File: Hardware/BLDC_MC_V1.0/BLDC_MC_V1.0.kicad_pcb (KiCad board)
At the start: 2 copper layers, 245 parts, among them J1 Conn_01x03_Pin, J2 Conn_01x03_Pin, J3 USB_C_Receptacle_USB2.0_16P, J4 Conn_02x03_Counter_Clockwise, J5 Conn_02x03_Counter_Clockwise, J6 1714971, J7 1714984, J8 430451012, Q1 BSC027N10NS5ATMA1, Q2 BSC027N10NS5ATMA1, Q3 BSC027N10NS5ATMA1, Q4 BSC027N10NS5ATMA1, Q5 BSC027N10NS5ATMA1, Q6 BSC027N10NS5ATMA1, Q7 BSC027N10NS5ATMA1, SW1 SW_Push, U1 LM76005RNPR, U10 TLV9061IDBVR, U11 TLV9061IDBVR, U12 TLV9061IDBVR, U13 TLV9061IDBVR, U14 TLV9061IDBVR, U15 TLV9061IDBVR, U16 LM74700QDRQ1, U2 TCAN334DR, U3 TLV9061IDBVR, U4 STM32G431RBT6, U5 LDL1117S33R, U6 DRV8353HRTAR, U7 NCV4274ADT50RKG, U8 25LC256-E_SN, U9 USBLC6-2SC6, Y1 7M-24.000MAAJ-T, Y2 ABS07-32.768KHZ-T

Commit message: Run DRC and solve all errors and warnings (project updated to Kicad 10)
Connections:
- J3 pad S1: GND -> (no net)

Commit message: Update recovery files of the project
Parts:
- removed TP11, TP12, TP13, TP14, TP15, TP16: TestPoint, Connector_Pin:Pin_D0.9mm_L10.0mm_W2.4mm_FlatFork
- moved Q6 154.0 mm to (129.2, 27.2), turned to 180 degrees
- moved R7 144.6 mm to (137.4, 33.5), turned to -90 degrees
- moved Q5 136.6 mm to (128.9, 41.3), turned to 180 degrees
- moved C65 132.3 mm to (228.6, 103.4)
- moved C66 132.3 mm to (235.7, 129.8)
- moved C84 132.3 mm to (244.6, 129.8)
- moved R26 132.3 mm to (214.1, 119.5)
- moved R29 132.3 mm to (214.1, 127.0)
- moved R32 132.3 mm to (218.1, 119.5)
- moved R56 132.3 mm to (235.5, 119.5)
- moved R60 132.3 mm to (235.5, 127.0)
- moved TP6 132.3 mm to (205.9, 119.0)
- moved TP7 132.3 mm to (205.9, 122.9)
- moved C10 132.3 mm to (161.9, 50.4)
- moved C12 132.3 mm to (253.4, 103.9)
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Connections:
- net Net-(C16-Pad1) renamed /BLDC_MC_V1.0_CAN_Transceiver/Split_CAP
- net Net-(U2-CANH) renamed /BLDC_MC_V1.0_CAN_Transceiver/CANH
- net Net-(U2-CANL) renamed /BLDC_MC_V1.0_CAN_Transceiver/CANL
- net Net-(U2-RXD) renamed /BLDC_MC_V1.0_CAN_Transceiver/IC_RXD
- net Net-(U2-SHDN) renamed /BLDC_MC_V1.0_CAN_Transceiver/SHDN
- net Net-(U2-STB) renamed /BLDC_MC_V1.0_CAN_Transceiver/STB
- net Net-(U2-TXD) renamed /BLDC_MC_V1.0_CAN_Transceiver/IC_TXD
- net Net-(U8-SI) renamed /BLDC_MC_V1.0_Memory/SI
- net Net-(U8-SO) renamed /BLDC_MC_V1.0_Memory/SO
- net Net-(U8-~CS) renamed /BLDC_MC_V1.0_Memory/CS
- net Net-(U8-~HOLD) renamed /BLDC_MC_V1.0_Memory/NHOLD
- net Net-(U8-~WP) renamed /BLDC_MC_V1.0_Memory/NWP
- R44 pad 1: /BLDC_MC_V1.0_MCU/SCK -> /BLDC_MC_V1.0_Memory/SCK
- R44 pad 2: Net-(U8-SCK) -> /BLDC_MC_V1.0_Memory/SCK
- U4 pad 19: /BLDC_MC_V1.0_MCU/SCK -> /BLDC_MC_V1.0_Memory/SCK
- U8 pad 6: Net-(U8-SCK) -> /BLDC_MC_V1.0_Memory/SCK
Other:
- board outline added: 131.4 x 64.3 mm
- copper layers 2 -> 8

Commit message: Update the plaacement of PCB
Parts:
- moved C11 220.5 mm to (38.4, 28.1)
- moved C12 220.5 mm to (47.0, 26.1)
- moved C13 220.5 mm to (38.1, 15.3)
- moved C14 220.5 mm to (38.1, 17.8)
- moved C15 220.5 mm to (38.1, 20.3)
- moved C16 220.5 mm to (38.1, 22.8)
- moved R9 220.5 mm to (38.1, 25.3)
- moved CR1 220.5 mm to (42.3, 28.1)
- moved R10 220.5 mm to (42.2, 15.3)
- moved R11 220.5 mm to (42.2, 17.8)
- moved R12 220.5 mm to (42.2, 20.3)
- moved R13 220.5 mm to (42.2, 22.8)
- moved R14 220.5 mm to (42.2, 25.3)
- moved FL1 216.4 mm to (52.7, 20.8), turned to 180 degrees
- moved U2 209.0 mm to (59.8, 20.8), turned to 180 degrees
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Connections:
- R44 pad 1: /BLDC_MC_V1.0_Memory/SCK -> /BLDC_MC_V1.0_MCU/SCK
- R44 pad 2: /BLDC_MC_V1.0_Memory/SCK -> /BLDC_MC_V1.0_Memory/SCK_M
- U4 pad 19: /BLDC_MC_V1.0_Memory/SCK -> /BLDC_MC_V1.0_MCU/SCK
- U8 pad 6: /BLDC_MC_V1.0_Memory/SCK -> /BLDC_MC_V1.0_Memory/SCK_M
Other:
- board size 131.4 x 64.3 mm -> 131.4 x 99.9 mm

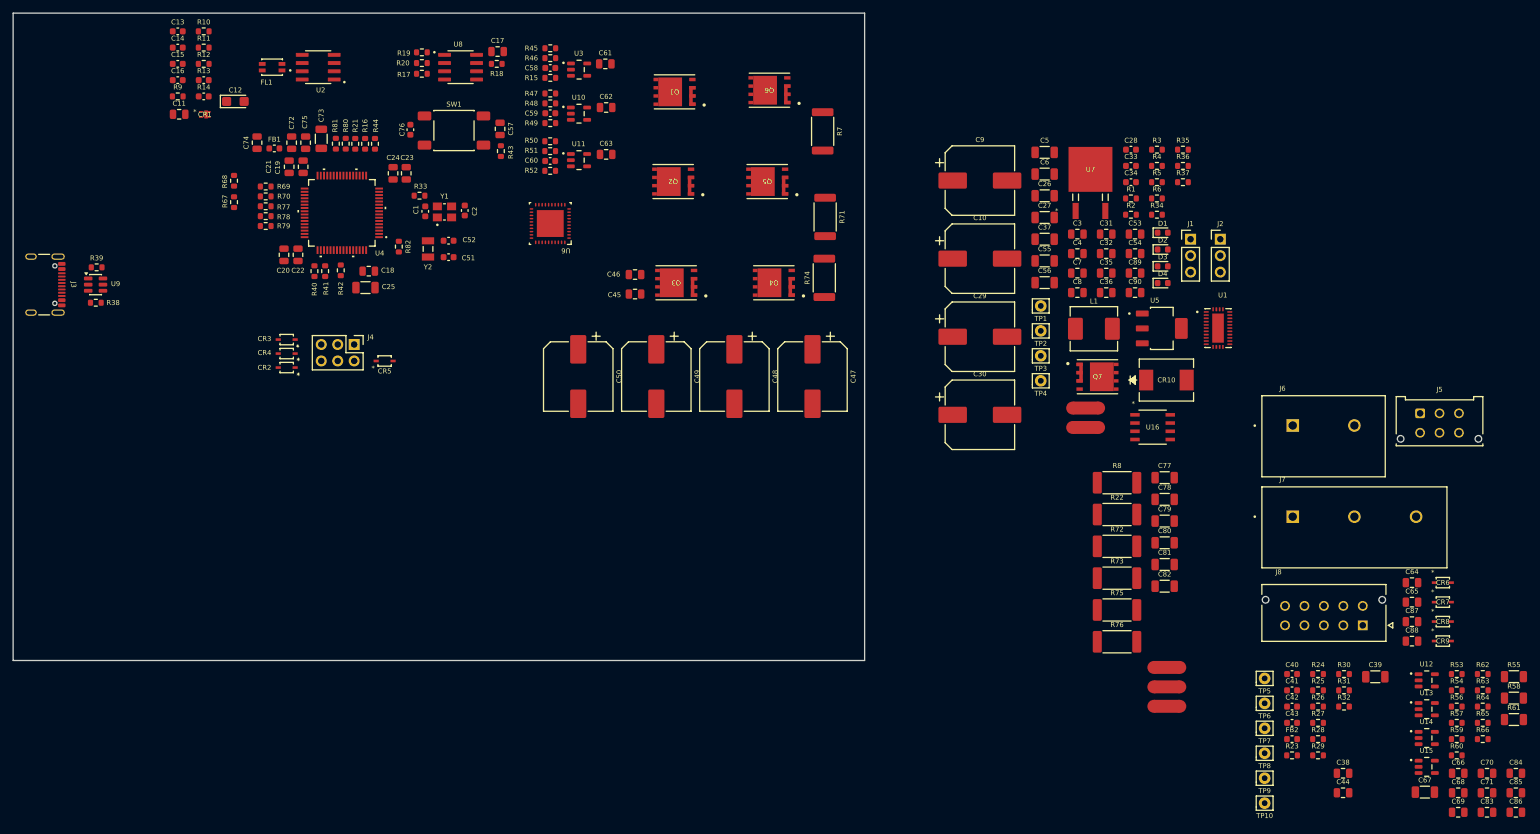
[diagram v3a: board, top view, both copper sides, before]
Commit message: Update the placement of the PCB
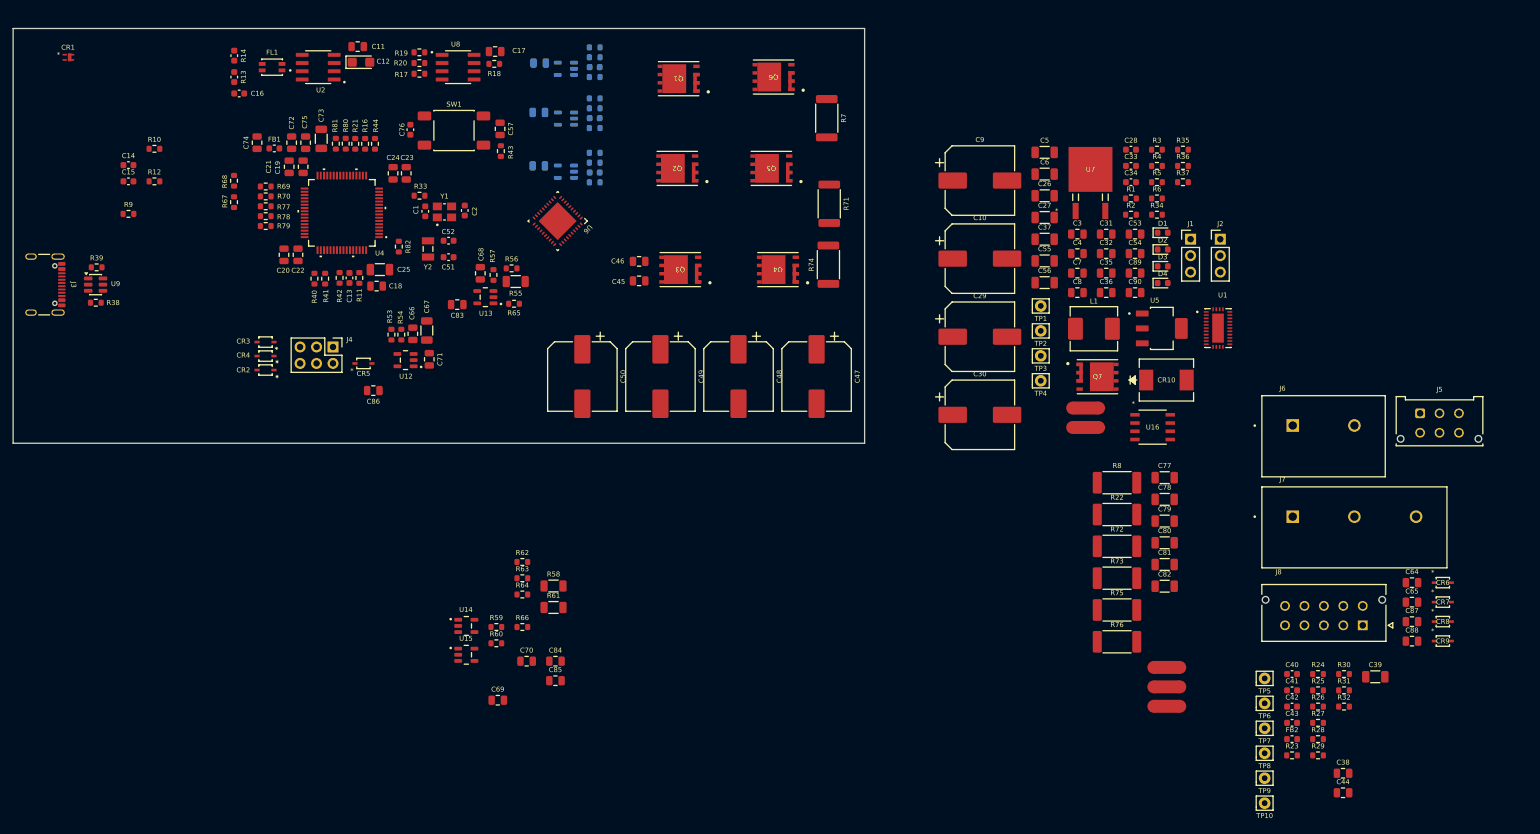
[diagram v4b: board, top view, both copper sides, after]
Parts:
- C58, C59, C60, C61, C62, C63, R15, R45, R46, R47, R48, R49, R50, R51, R52, U10, U11, U3: moved to B.Cu
- moved C86 187.9 mm to (68.3, 70.7), turned to 180 degrees
- moved C83 177.2 mm to (81.3, 57.5), turned to 180 degrees
- moved C71 176.4 mm to (77.0, 65.9), turned to 90 degrees
- moved C66 175.0 mm to (74.4, 62.0), turned to 90 degrees
- moved R53 172.6 mm to (71.1, 62.1), turned to 90 degrees
- moved R54 171.9 mm to (72.6, 62.1), turned to -90 degrees
- moved C68 170.9 mm to (84.8, 52.6), turned to 90 degrees
- moved C67 169.7 mm to (76.6, 61.5), turned to 90 degrees
- moved R55 165.7 mm to (90.3, 53.9), turned to 180 degrees
- moved U12 165.2 mm to (73.3, 66.0), turned to 180 degrees
- moved R57 163.9 mm to (86.9, 52.9), turned to 90 degrees
- moved R65 162.9 mm to (90.0, 57.3), turned to 180 degrees
- moved R56 160.8 mm to (89.7, 51.9)
- moved U13 158.6 mm to (85.6, 56.3), turned to 180 degrees
- moved C69 149.2 mm to (87.5, 118.5)
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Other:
- board size 131.4 x 99.9 mm -> 131.4 x 64 mm

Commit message: Update the placement of the board
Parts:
- removed TP10, TP5, TP6, TP7, TP8, TP9: TestPoint, Connector_Pin:Pin_D0.9mm_L10.0mm_W2.4mm_FlatFork
- C47, C48, C49, C50, C66, C67, C71, C86, R53, R54, U12: moved to B.Cu
- moved C44 158.0 mm to (96.5, 31.8), turned to 135 degrees
- moved R29 152.5 mm to (89.7, 38.9), turned to -45 degrees
- moved R28 151.0 mm to (87.7, 42.0)
- moved R32 150.1 mm to (95.4, 33.1), turned to -45 degrees
- moved R27 149.3 mm to (90.9, 37.7), turned to -45 degrees
- moved R31 149.2 mm to (93.2, 35.4), turned to -45 degrees
- moved R26 149.1 mm to (87.7, 40.5)
- moved R30 148.2 mm to (92.0, 36.6), turned to -45 degrees
- moved R25 145.6 mm to (94.3, 34.3), turned to -45 degrees
- moved R23 144.3 mm to (92.5, 43.6), turned to 45 degrees
- moved R24 142.4 mm to (91.3, 42.4), turned to 45 degrees
- moved C38 140.7 mm to (102.4, 49.4), turned to -45 degrees
- moved FB2 140.1 mm to (92.6, 48.3), turned to -45 degrees
- moved C39 135.9 mm to (104.5, 48.3), turned to 135 degrees
- moved C43 135.9 mm to (96.5, 47.5), turned to 45 degrees
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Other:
- board size 131.4 x 64 mm -> 137 x 50 mm

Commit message: Update the component placement of the board
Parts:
- removed C14, C15: 10pF, Capacitor_SMD:C_0603_1608Metric
- removed R10, R9: 33R, Resistor_SMD:R_0603_1608Metric
- added H1: MountingHole_Pad, MountingHole:MountingHole_2.2mm_M2_Pad_Via, F.Cu at (40.5, 65.4)
- added H2: MountingHole_Pad, MountingHole:MountingHole_2.2mm_M2_Pad_Via, F.Cu at (40.4, 16.8)
- added H3: MountingHole_Pad, MountingHole:MountingHole_2.2mm_M2_Pad_Via, F.Cu at (154.8, 65.5)
- added H4: MountingHole_Pad, MountingHole:MountingHole_2.2mm_M2_Pad_Via, F.Cu at (154.8, 16.8)
- C10, C17, C29, C30, C68, C69, C70, C83, C84, C85, C88, C9, CR7, CR8, CR9, R17, R18, R19, R20, R55, R56, R57, R58, R59, R60, R61, R62, R63, R64, R65, R66, U13, U14, U15, U8: moved to B.Cu
- J5: value Conn_02x03_Counter_Clockwise -> S6B-PH-K-S_LF__SN_; footprint Connector_Molex:Molex_Micro-Fit_3.0_43045-0612_2x03_P3.00mm_Vertical -> BLDC_Motor_Driver_Components_Footprint:JST_S6B-PH-K-S_LF__SN_
- J6: value 1714971 -> XT60-M; footprint BLDC_Motor_Driver_Components_Footprint:PHOENIX_1714971 -> BLDC_Motor_Driver_Components_Footprint:AMASS_XT60-M
- J8: value 430451012 -> S10B-PHDSS LFSN; footprint BLDC_Motor_Driver_Components_Footprint:MOLEX_430451012 -> BLDC_Motor_Driver_Components_Footprint:CONN_S10B-PHDSS_JST
- moved CR9 244.6 mm to (40.3, 46.4), turned to 180 degrees
- moved CR8 244.3 mm to (40.3, 44.3), turned to 180 degrees
- moved CR7 244.0 mm to (40.3, 42.2), turned to 180 degrees
- moved C88 242.7 mm to (40.1, 40.0), turned to 180 degrees
- moved C87 235.0 mm to (48.0, 38.2), turned to 90 degrees
- moved CR6 232.7 mm to (49.7, 46.4)
- moved J8 229.6 mm to (45.7, 40.2), turned to -90 degrees
- moved J6 219.8 mm to (42.4, 28.2), turned to -90 degrees
- moved C64 173.6 mm to (91.1, 109.3)
- moved C65 173.6 mm to (91.1, 112.4)
- moved C26 166.8 mm to (51.0, 87.5)
- moved C27 166.8 mm to (51.0, 90.9)
- moved C28 166.8 mm to (64.3, 80.4)
- moved C3 166.8 mm to (56.0, 93.4)
- moved C31 166.8 mm to (60.5, 93.4)
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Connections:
- C90 pad 2: /BLDC_MC_V1.0_Connectors/GND_In -> GND
- CR10 pad 2: /BLDC_MC_V1.0_Connectors/GND_In -> GND
- J5 pad 3: GND -> /BLDC_MC_V1.0_Connectors/Hall_B
- J5 pad 5: /BLDC_MC_V1.0_Connectors/Hall_B -> +3.3V
- J5 pad 6: +3.3V -> GND
- U16 pad 1: /BLDC_MC_V1.0_Connectors/GND_In -> GND
- U4 pad 58: /BLDC_MC_V1.0_CAN_Transceiver/CAN_STB -> /BLDC_MC_V1.0_CAN_Transceiver/STB
- U4 pad 59: /BLDC_MC_V1.0_CAN_Transceiver/CAN_SHDN -> /BLDC_MC_V1.0_CAN_Transceiver/SHDN
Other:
- board size 137 x 50 mm -> 120 x 55 mm

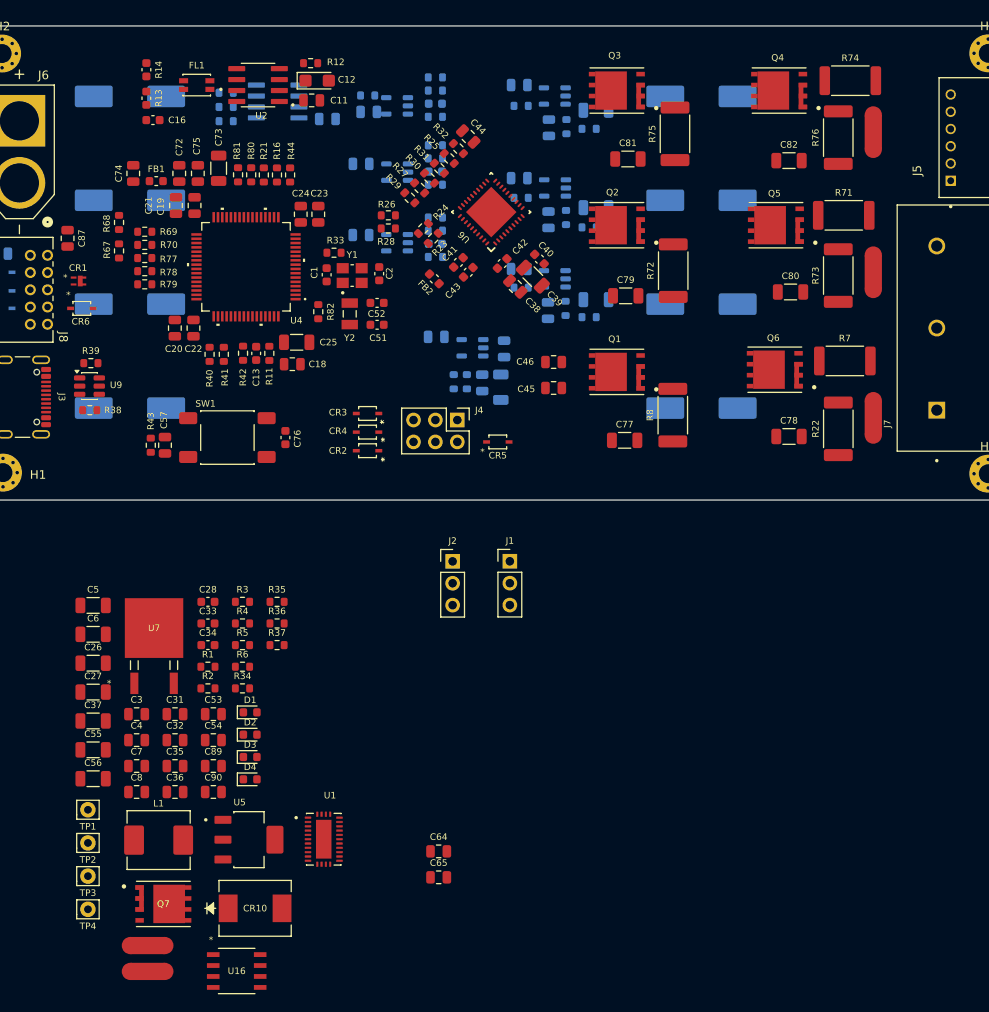
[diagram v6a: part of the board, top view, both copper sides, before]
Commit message: Update the components' placement of the board
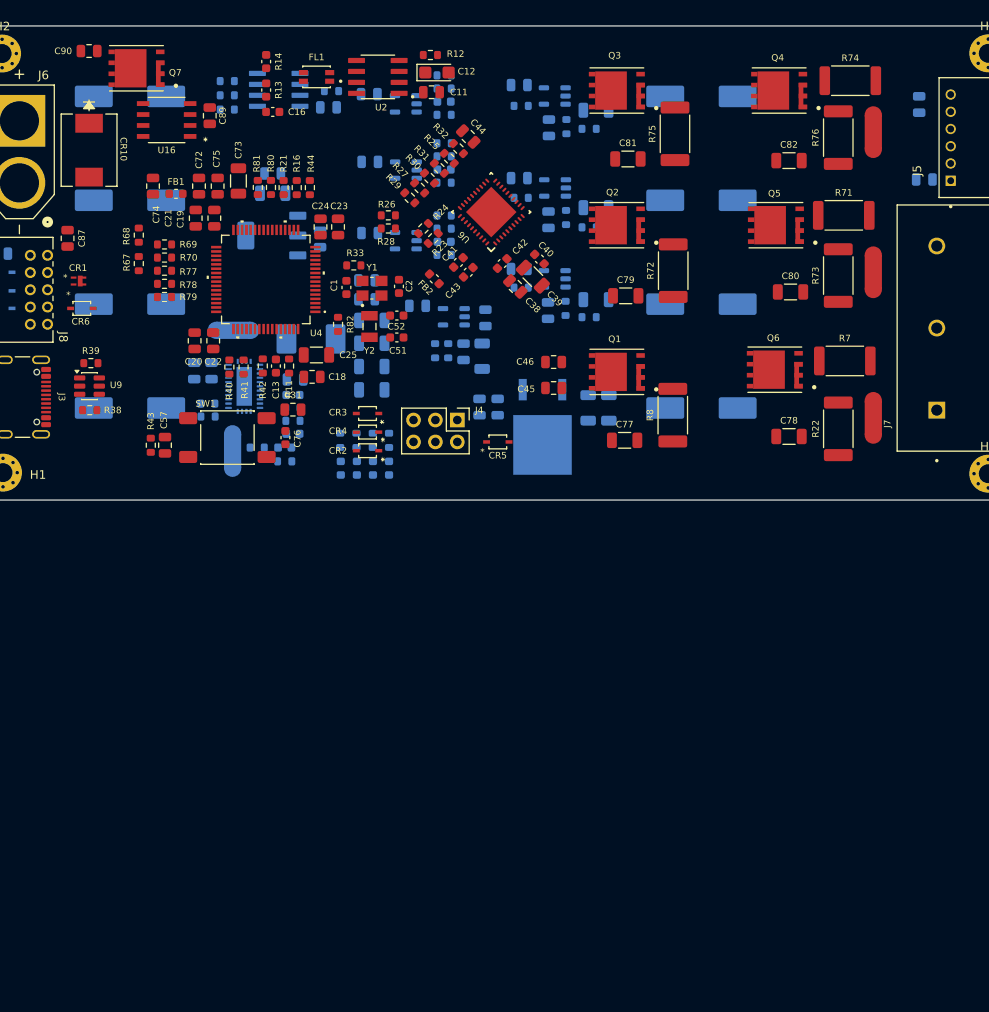
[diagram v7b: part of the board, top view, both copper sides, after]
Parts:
- removed J1, J2: Conn_01x03_Pin, Connector_PinHeader_2.54mm:PinHeader_1x03_P2.54mm_Vertical
- removed TP1, TP2, TP3, TP4: TestPoint, Connector_Pin:Pin_D0.9mm_L10.0mm_W2.4mm_FlatFork
- C26, C27, C28, C3, C32, C33, C34, C35, C36, C37, C4, C5, C53, C54, C55, C56, C6, C64, C65, C7, C8, D1, D2, D3, D4, L1, NT4, NT5, R1, R2, R3, R34, R35, R36, R37, R4, R5, R6, U1, U5, U7: moved to B.Cu
- moved C64 103.0 mm to (146.8, 22.7), turned to 90 degrees
- moved U16 99.1 mm to (59.5, 24.5), turned to 180 degrees
- moved C65 98.6 mm to (147.4, 31.4), turned to 180 degrees
- moved Q7 97.0 mm to (56.0, 18.5), turned to 180 degrees
- moved CR10 90.0 mm to (50.5, 28.0), turned to -90 degrees
- moved C90 87.2 mm to (50.5, 16.5), turned to 180 degrees
- moved C89 75.4 mm to (64.5, 24.0), turned to 90 degrees
- moved NT5 75.0 mm to (67.2, 48.9), turned to 180 degrees
- moved C56 73.7 mm to (110.8, 57.9), turned to -90 degrees
- moved U5 70.1 mm to (71.7, 37.9), turned to 180 degrees
- moved C55 69.8 mm to (108.4, 57.9), turned to -90 degrees
- moved C35 69.7 mm to (71.8, 30.7)
- moved C36 66.3 mm to (77.3, 38.3), turned to 90 degrees
- moved C37 64.7 mm to (71.8, 33.0)
- moved L1 60.8 mm to (76.2, 49.9)
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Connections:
- C36 pad 1: Net-(J1-Pin_2) -> +12V
- C53 pad 1: Net-(J2-Pin_2) -> +12V
- C54 pad 1: Net-(J2-Pin_2) -> +12V
- U5 pad 3: Net-(J1-Pin_2) -> +12V
- U7 pad 1: Net-(J2-Pin_2) -> +12V
